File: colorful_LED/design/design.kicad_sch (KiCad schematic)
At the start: 14 parts, among them J1 USB_B, SW1 SW_Push, U1 ATmega32U4-A, Y1 8MHz

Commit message: Added some footprints
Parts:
- FB1: footprint (none) -> Inductor_SMD:L_0603_1608Metric_Pad1.05x0.95mm_HandSolder
- R4: value 22 -> 10k
- SW1: footprint (none) -> Button_Switch_SMD:SW_Push_1TS009xxxx-xxxx-xxxx_6x6x5mm
- Y1: footprint (none) -> Crystal:Crystal_SMD_HC49-SD_HandSoldering
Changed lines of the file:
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@@
 			)
 		)
-		(property "Footprint" ""
+		(property "Footprint" "Inductor_SMD:L_0603_1608Metric_Pad1.05x0.95mm_HandSolder"
 			(at 220.472 41.91 90)
 			(effects
@@
 			)
 		)
-		(property "Footprint" ""
+		(property "Footprint" "Button_Switch_SMD:SW_Push_1TS009xxxx-xxxx-xxxx_6x6x5mm"
 			(at 196.85 44.45 0)
 			(effects
@@
 			)
 		)
-		(property "Value" "22"
+		(property "Value" "10k"
 			(at 205.74 44.196 90)
 			(effects
@@
 			)
 		)
-		(property "Footprint" ""
+		(property "Footprint" "Crystal:Crystal_SMD_HC49-SD_HandSoldering"
 			(at 198.12 62.23 0)
 			(effects

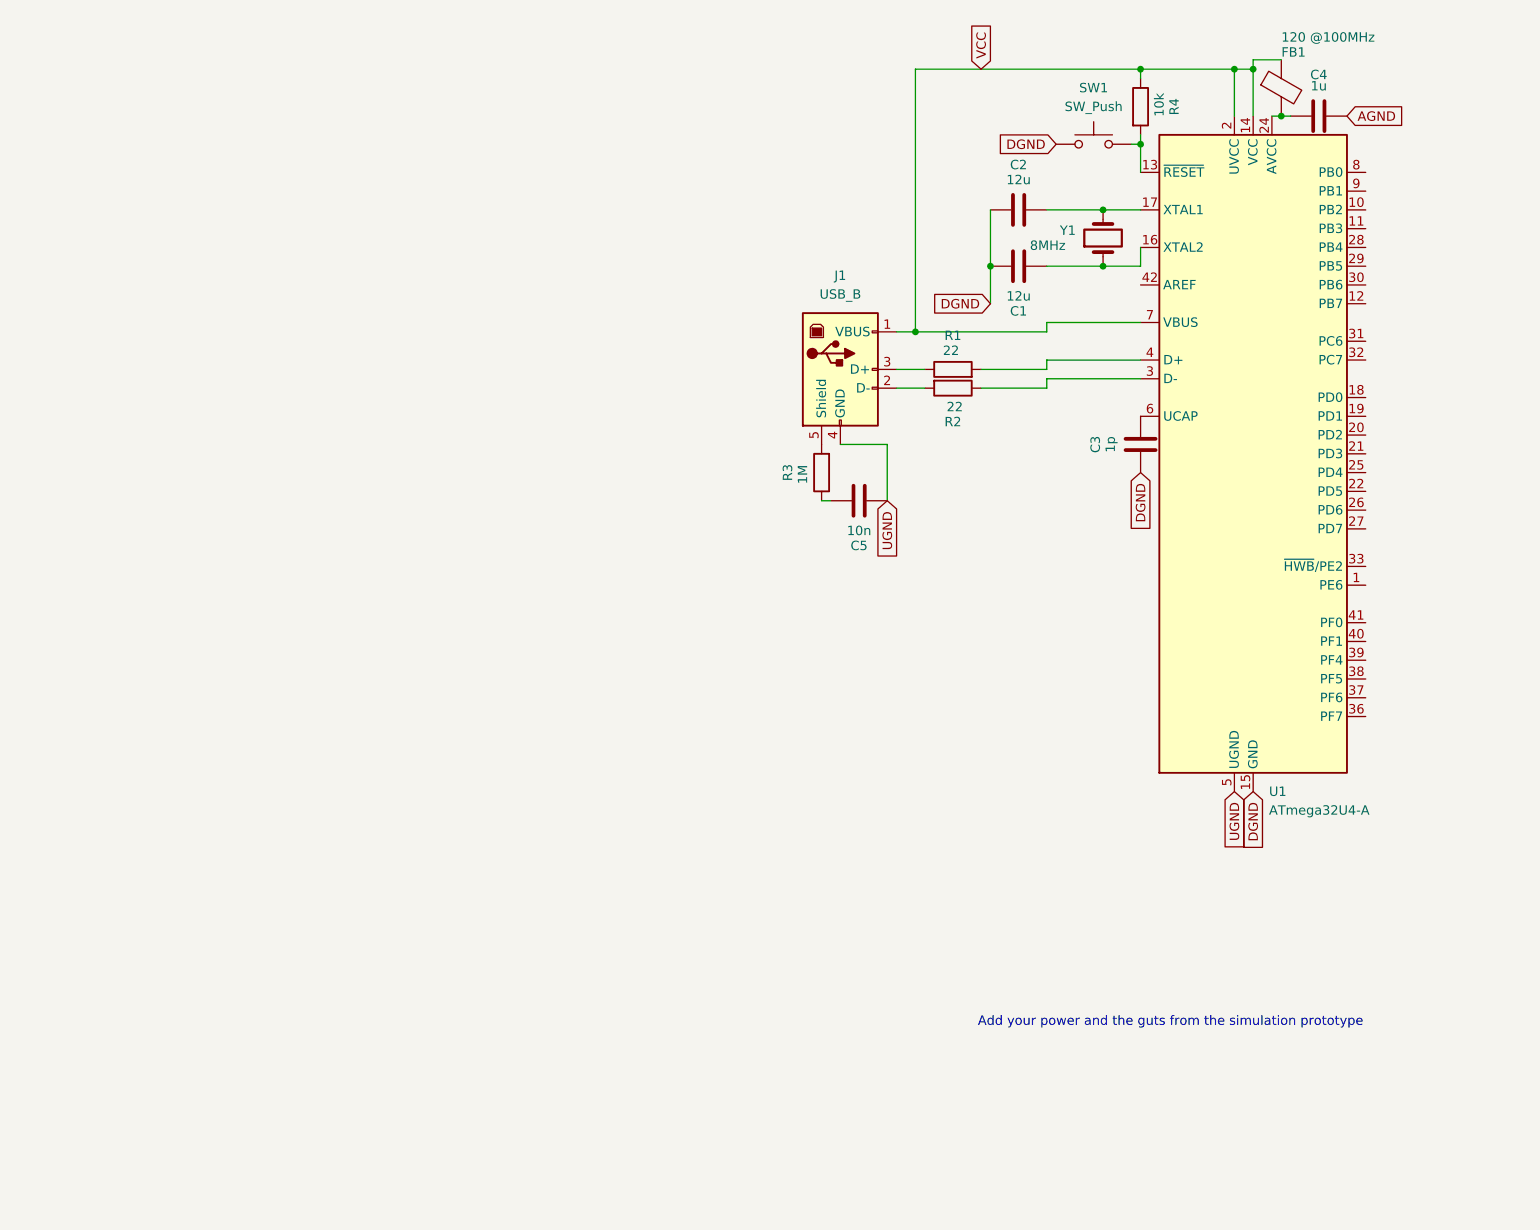
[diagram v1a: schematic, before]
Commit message: worked on schematic and added boost converter to custom lib
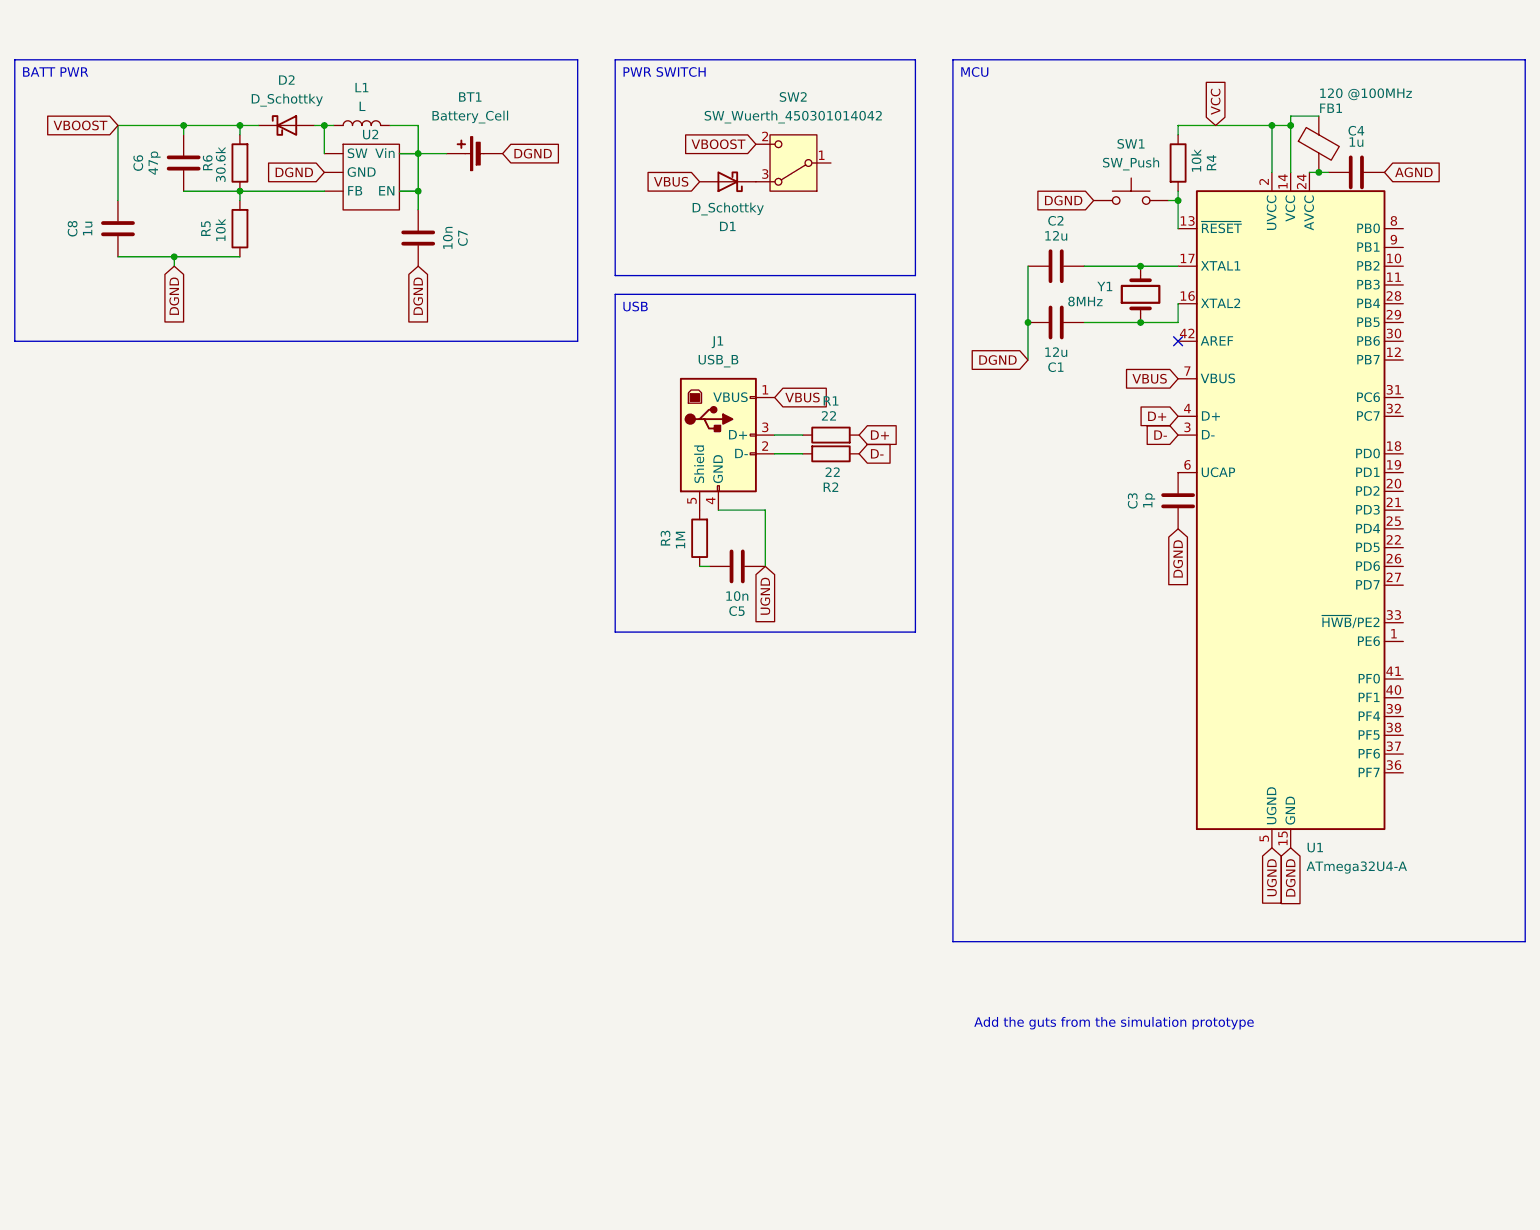
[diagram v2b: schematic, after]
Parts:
- added BT1: Battery_Cell, Battery:BatteryHolder_ComfortableElectronic_CH273-2450_1x2450, symbol Device:Battery_Cell
- added C6: 47p, Capacitor_SMD:C_0805_2012Metric, symbol Device:C
- added C7: 10n, Capacitor_SMD:C_0805_2012Metric, symbol Device:C
- added C8: 1u, Capacitor_SMD:C_0805_2012Metric, symbol Device:C
- added D1, D2: D_Schottky, Diode_SMD:D_0805_2012Metric, symbol Device:D_Schottky
- added L1: L, Inductor_SMD:L_0805_2012Metric, symbol Device:L
- added R5: 10k, Resistor_SMD:R_0805_2012Metric, symbol Device:R
- added R6: 30.6k, Resistor_SMD:R_0805_2012Metric, symbol Device:R
- added SW2: SW_Wuerth_450301014042, Button_Switch_THT:SW_Slide-03_Wuerth-WS-SLTV_10x2.5x6.4_P2.54mm, symbol Switch:SW_Wuerth_450301014042
- added U2: ~, Colorful_LED:Reg, symbol Colorful_LED:Reg_1
- J1: footprint (none) -> Connector_USB:USB_B_Lumberg_2411_02_Horizontal
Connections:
- net DGND: now also BT1.2 (-), C7.1, C8.2, R5.1, U2. (EN)
- net VCC: no longer J1.1 (VBUS), U1.7 (VBUS)
- net D-: now reaches R2.1, U1.3 (D-)
- net D+: now reaches R1.2, U1.4 (D+)
- new net: C6.2, R5.2, R6.1, U2. (EN)
- new net: D1.1 (K), SW2.3 (A)
- new net: D2.2 (A), L1.1, U2. (EN)
- new net: BT1.1 (+), C7.2, L1.2, U2. (EN)
- new net VBOOST: C6.1, C8.1, D2.1 (K), R6.2, SW2.2 (C)
- new net VBUS: D1.2 (A), J1.1 (VBUS), U1.7 (VBUS)
- no-connect marks 0 -> 1
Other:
- note added: "Add the guts from the simulation prototype"
- note removed: "Add your power and the guts from the simulation prototype"
- moved on the sheet: C1, C2, C3, C4, C5, FB1, J1, R1, R2, R3, R4, SW1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

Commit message: Finished analog
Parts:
- added D3: LED_BGRK, symbol Device:LED_BGRK
- added DS1: OLED-128O064D, Display:OLED-128O064D, symbol Display_Graphic:OLED-128O064D
- added R7, R8, R9: 220, Resistor_SMD:R_0805_2012Metric, symbol Device:R
- added RV1, RV2, RV3: R_Potentiometer, Potentiometer_SMD:Potentiometer_ACP_CA6-VSMD_Vertical, symbol Device:R_Potentiometer
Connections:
- net AGND: now also D3.4 (K), RV1.3, RV2.3, RV3.3
- net AVCC: now reaches C4.2, FB1.2, U1.24 (AVCC), U1.44 (AVCC)
- net AVCC: now also RV1.1, RV2.1, RV3.1
- net B_LEG: now reaches U1.10 (PB2)
- net B_LEG: now also R9.1
- net SCL: now reaches U1.18 (PD0)
- net SDA: now reaches U1.19 (PD1)
- net B_POT: now reaches U1.39 (PF4)
- net B_POT: now also RV3.2
- net G_POT: now reaches U1.40 (PF1)
- net G_POT: now also RV2.2
- net R_POT: now reaches U1.41 (PF0)
- net R_POT: now also RV1.2
- net R_LEG: now reaches U1.8 (PB0)
- net R_LEG: now also R7.1
- net G_LEG: now reaches U1.9 (PB1)
- net G_LEG: now also R8.1
- new net: D3.2 (GA), R8.2
- new net: D3.3 (RA), R7.2
- new net: DS1.1 (GND), DS1.30 (GND)
- new net: D3.1 (BA), R9.2
- no-connect marks 1 -> 19
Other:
- moved on the sheet: FB1

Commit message: Finished Schematic
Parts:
- added D4: G_ON, LED_SMD:LED_0805_2012Metric, symbol Device:LED
- added R10, R11: 4.7k, Resistor_SMD:R_0805_2012Metric, symbol Device:R
- added R12: 220, Resistor_SMD:R_0805_2012Metric, symbol Device:R
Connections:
- net DGND: now also DS1.1 (GND), DS1.10 (BS0), DS1.30 (GND), U2.2 (GND), D4.1 (K); no longer U2. (EN)
- net SCL: now also DS1.18 (D0), R11.2
- net SDA: now also DS1.19 (D1), DS1.20 (D2), R10.1
- net VCC: now also DS1.28 (VCC), SW2.1 (B), R10.2, R11.1, R12.2
- net at C6.2, R5.2, R6.1: now also U2.3 (FB); no longer U2. (EN)
- net at D2.2 (A), L1.1: now also U2.1 (SW); no longer U2. (EN)
- net at BT1.1 (+), C7.2, L1.2: now also U2.4 (EN), U2.5 (Vin); no longer U2. (EN)
- new net: D4.2 (A), R12.1
- no-connect marks 19 -> 41
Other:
- note removed: "Add the guts from the simulation prototype"
- moved on the sheet: BT1, C1, C2, C3, C4, C5, C6, C7, C8, D1, D2, D3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

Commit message: Added last footprint tht
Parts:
- removed D3: LED_BGRK, symbol Device:LED_BGRK
- added D5: LED_BKGR, LED_THT:LED_D5.0mm-4_RGB, symbol Device:LED_BKGR
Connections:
- net AGND: now also D5.2 (K)
- net B_LEG: now also R8.1; no longer R9.1
- net G_LEG: now also R9.1; no longer R8.1
- net at R8.2: now also D5.3 (GA)
- net at R7.2: now also D5.4 (RA)
- net at R9.2: now also D5.1 (BA)
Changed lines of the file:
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@@
 	(global_label "G_LEG"
 		(shape input)
-		(at 101.6 105.41 0)
+		(at 101.6 113.03 0)
 		(fields_autoplaced yes)
 		(effects
@@
 		)
 		(property "Intersheetrefs" "${INTERSHEET_REFS}"
-			(at 110.2699 105.41 0)
+			(at 110.2699 113.03 0)
 			(effects
 				(font
@@
 	(global_label "B_LEG"
 		(shape input)
-		(at 101.6 113.03 0)
+		(at 101.6 105.41 0)
 		(fields_autoplaced yes)
 		(effects
@@
 		)
 		(property "Intersheetrefs" "${INTERSHEET_REFS}"
-			(at 110.2699 113.03 0)
+			(at 110.2699 105.41 0)
 			(effects
 				(font
@@
 	)
 	(symbol
-		(lib_id "Device:LED_BGRK")
+		(lib_id "Device:LED_BKGR")
 		(at 80.01 105.41 0)
 		(unit 1)
@@
 		(dnp no)
 		(fields_autoplaced yes)
-		(property "Reference" "D3"
+		(property "Reference" "D5"
 			(at 80.01 91.44 0)
 			(effects
@@
 			)
 		)
-		(property "Value" "LED_BGRK"
+		(property "Value" "LED_BKGR"
 			(at 80.01 93.98 0)
 			(effects
@@
 			)
 		)
-		(property "Footprint" ""
+		(property "Footprint" "LED_THT:LED_D5.0mm-4_RGB"
 			(at 80.01 106.68 0)
 			(effects
@@
 			)
 		)
-		(property "Description" "RGB LED, blue/green/red/cathode"
+		(property "Description" "RGB LED, blue/cathode/green/red"
 			(at 80.01 105.41 0)
 			(effects
@@
 			)
 		)
+		(pin "2"
+		)
 		(pin "4"
 		)
 		(pin "3"
 		)
-		(pin "2"
-		)
 		(pin "1"
 		)
@@
 			(project ""
 				(path "/94c6f3db-6cf1-4f7f-a924-011f14387f61"
-					(reference "D3")
+					(reference "D5")
 					(unit 1)
 				)

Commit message: Fixed some minor bugs
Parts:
- C1, C2: footprint (none) -> Capacitor_SMD:C_0805_2012Metric
- L1: value L -> 10u
- RV1, RV2, RV3: footprint Potentiometer_SMD:Potentiometer_ACP_CA6-VSMD_Vertical -> Potentiometer_SMD:Potentiometer_Bourns_3314S_Horizontal
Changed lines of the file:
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@@
+	)
+	(symbol
+		(lib_id "Device:R_Potentiometer")
+		(at 105.41 87.63 0)
+		(unit 1)
+		(exclude_from_sim no)
+		(in_bom yes)
+		(on_board yes)
+		(dnp no)
+		(property "Reference" "RV3"
+			(at 102.87 88.9001 0)
+			(effects
+				(font
+					(size 1.27 1.27)
+				)
+				(justify right)
+			)
+		)
+		(property "Value" "R_Potentiometer"
+			(at 112.522 96.012 0)
+			(effects
+				(font
+					(size 1.27 1.27)
+				)
+				(justify right)
+				(hide yes)
+			)
+		)
+		(property "Footprint" "Potentiometer_SMD:Potentiometer_Bourns_3314S_Horizontal"
+			(at 105.41 87.63 0)
+			(effects
+				(font
+					(size 1.27 1.27)
+				)
+				(hide yes)
+			)
+		)
+		(property "Datasheet" "~"
+			(at 105.41 87.63 0)
+			(effects
+				(font
+					(size 1.27 1.27)
+				)
+				(hide yes)
+			)
+		)
+		(property "Description" "Potentiometer"
+			(at 105.41 87.63 0)
+			(effects
+				(font
+					(size 1.27 1.27)
+				)
+				(hide yes)
+			)
+		)
+		(pin "1"
+		)
+		(pin "2"
+		)
+		(pin "3"
+		)
+		(instances
+			(project "design"
+				(path "/94c6f3db-6cf1-4f7f-a924-011f14387f61"
+					(reference "RV3")
+					(unit 1)
+				)
+			)
+		)
 	)
 	(symbol
@@
 	)
 	(symbol
-		(lib_id "Device:R_Potentiometer")
-		(at 63.5 87.63 0)
-		(unit 1)
-		(exclude_from_sim no)
-		(in_bom yes)
-		(on_board yes)
-		(dnp no)
-		(property "Reference" "RV1"
-			(at 60.96 88.9001 0)
-			(effects
-				(font
-					(size 1.27 1.27)
-				)
-				(justify right)
-			)
-		)
-		(property "Value" "R_Potentiometer"
-			(at 70.612 96.012 0)
-			(effects
-				(font
-					(size 1.27 1.27)
-				)
-				(justify right)
-				(hide yes)
-			)
-		)
-		(property "Footprint" "Potentiometer_SMD:Potentiometer_ACP_CA6-VSMD_Vertical"
-			(at 63.5 87.63 0)
-			(effects
-				(font
-					(size 1.27 1.27)
-				)
-				(hide yes)
-			)
-		)
-		(property "Datasheet" "~"
-			(at 63.5 87.63 0)
-			(effects
-				(font
-					(size 1.27 1.27)
-				)
-				(hide yes)
-			)
-		)
-		(property "Description" "Potentiometer"
-			(at 63.5 87.63 0)
-			(effects
-				(font
-					(size 1.27 1.27)
-				)
-				(hide yes)
-			)
-		)
-		(pin "1"
-		)
-		(pin "2"
-		)
-		(pin "3"
-		)
-		(instances
-			(project ""
-				(path "/94c6f3db-6cf1-4f7f-a924-011f14387f61"
-					(reference "RV1")
-					(unit 1)
-				)
-			)
-		)
-	)
-	(symbol
 		(lib_id "Device:C")
 		(at 193.04 73.66 90)
@@
 			)
 		)
-		(property "Footprint" ""
+		(property "Footprint" "Capacitor_SMD:C_0805_2012Metric"
 			(at 196.85 72.6948 0)
 			(effects
@@
 				(path "/94c6f3db-6cf1-4f7f-a924-011f14387f61"
 					(reference "R2")
-					(unit 1)
-				)
-			)
-		)
-	)
-	(symbol
-		(lib_id "Device:R_Potentiometer")
-		(at 105.41 87.63 0)
-		(unit 1)
-		(exclude_from_sim no)
-		(in_bom yes)
-		(on_board yes)
-		(dnp no)
-		(property "Reference" "RV3"
-			(at 102.87 88.9001 0)
-			(effects
-				(font
-					(size 1.27 1.27)
-				)
-				(justify right)
-			)
-		)
-		(property "Value" "R_Potentiometer"
-			(at 112.522 96.012 0)
-			(effects
-				(font
-					(size 1.27 1.27)
-				)
-				(justify right)
-				(hide yes)
-			)
-		)
-		(property "Footprint" "Potentiometer_SMD:Potentiometer_ACP_CA6-VSMD_Vertical"
-			(at 105.41 87.63 0)
-			(effects
-				(font
-					(size 1.27 1.27)
-				)
-				(hide yes)
-			)
-		)
-		(property "Datasheet" "~"
-			(at 105.41 87.63 0)
-			(effects
-				(font
-					(size 1.27 1.27)
-				)
-				(hide yes)
-			)
-		)
-		(property "Description" "Potentiometer"
-			(at 105.41 87.63 0)
-			(effects
-				(font
-					(size 1.27 1.27)
-				)
-				(hide yes)
-			)
-		)
-		(pin "1"
-		)
-		(pin "2"
-		)
-		(pin "3"
-		)
-		(instances
-			(project "design"
-				(path "/94c6f3db-6cf1-4f7f-a924-011f14387f61"
-					(reference "RV3")
 					(unit 1)
 				)
@@
 			)
 		)
-		(property "Footprint" ""
+		(property "Footprint" "Capacitor_SMD:C_0805_2012Metric"
 			(at 196.85 65.0748 0)
 			(effects
@@
 			)
 		)
-		(property "Footprint" "Potentiometer_SMD:Potentiometer_ACP_CA6-VSMD_Vertical"
+		(property "Footprint" "Potentiometer_SMD:Potentiometer_Bourns_3314S_Horizontal"
 			(at 85.09 87.63 0)
 			(effects
@@
 				(path "/94c6f3db-6cf1-4f7f-a924-011f14387f61"
 					(reference "R10")
+					(unit 1)
+				)
+			)
+		)
+	)
+	(symbol
+		(lib_id "Device:R_Potentiometer")
+		(at 63.5 87.63 0)
+		(unit 1)
+		(exclude_from_sim no)
+		(in_bom yes)
+		(on_board yes)
+		(dnp no)
+		(property "Reference" "RV1"
+			(at 60.96 88.9001 0)
+			(effects
+				(font
+					(size 1.27 1.27)
+				)
+				(justify right)
+			)
+		)
+		(property "Value" "R_Potentiometer"
+			(at 70.612 96.012 0)
+			(effects
+				(font
+					(size 1.27 1.27)
+				)
+				(justify right)
+				(hide yes)
+			)
+		)
+		(property "Footprint" "Potentiometer_SMD:Potentiometer_Bourns_3314S_Horizontal"
+			(at 63.5 87.63 0)
+			(effects
+				(font
+					(size 1.27 1.27)
+				)
+				(hide yes)
+			)
+		)
+		(property "Datasheet" "~"
+			(at 63.5 87.63 0)
+			(effects
+				(font
+					(size 1.27 1.27)
+				)
+				(hide yes)
+			)
+		)
+		(property "Description" "Potentiometer"
+			(at 63.5 87.63 0)
+			(effects
+				(font
+					(size 1.27 1.27)
+				)
+				(hide yes)
+			)
+		)
+		(pin "1"
+		)
+		(pin "2"
+		)
+		(pin "3"
+		)
+		(instances
+			(project "design"
+				(path "/94c6f3db-6cf1-4f7f-a924-011f14387f61"
+					(reference "RV1")
 					(unit 1)
 				)
@@
 			)
 		)
-		(property "Value" "L"
+		(property "Value" "10u"
 			(at 97.79 40.64 90)
 			(effects
